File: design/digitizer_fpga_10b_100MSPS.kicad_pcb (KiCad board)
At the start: 4 copper layers, 110 x 60 mm, 281 parts, among them J1 POWER, J2 SWD_01X04, J3 DEBUG_SPI, J4 USB_B_Mini, J5 SMA, J6 JUMPER_DFS/GAIN, J7 DEBUG_FPGA_GPIO, J8 DIGILENT_JTAG_HS2_01X06, SW1 RST, SW2 PROG, U1 LM3880MF-1AA, U10 IS61WV12816EDBLL-10TLI, U11 TLV431ACDBZR, U12 AD9214, U13 XC7S15-FTGB196, U14 IS25LP064A-JKx, U2 NCP59744MN1, U3 NCP59744MN1, U4 NCP59744MN1, U5 NCP59744MN1, U6 STM32H750VBTx, U7 USBLC6-2SC6, U8 FT231XS, U9 ADA4930-1, X1 ASTX-H11-25.000MHZ-T

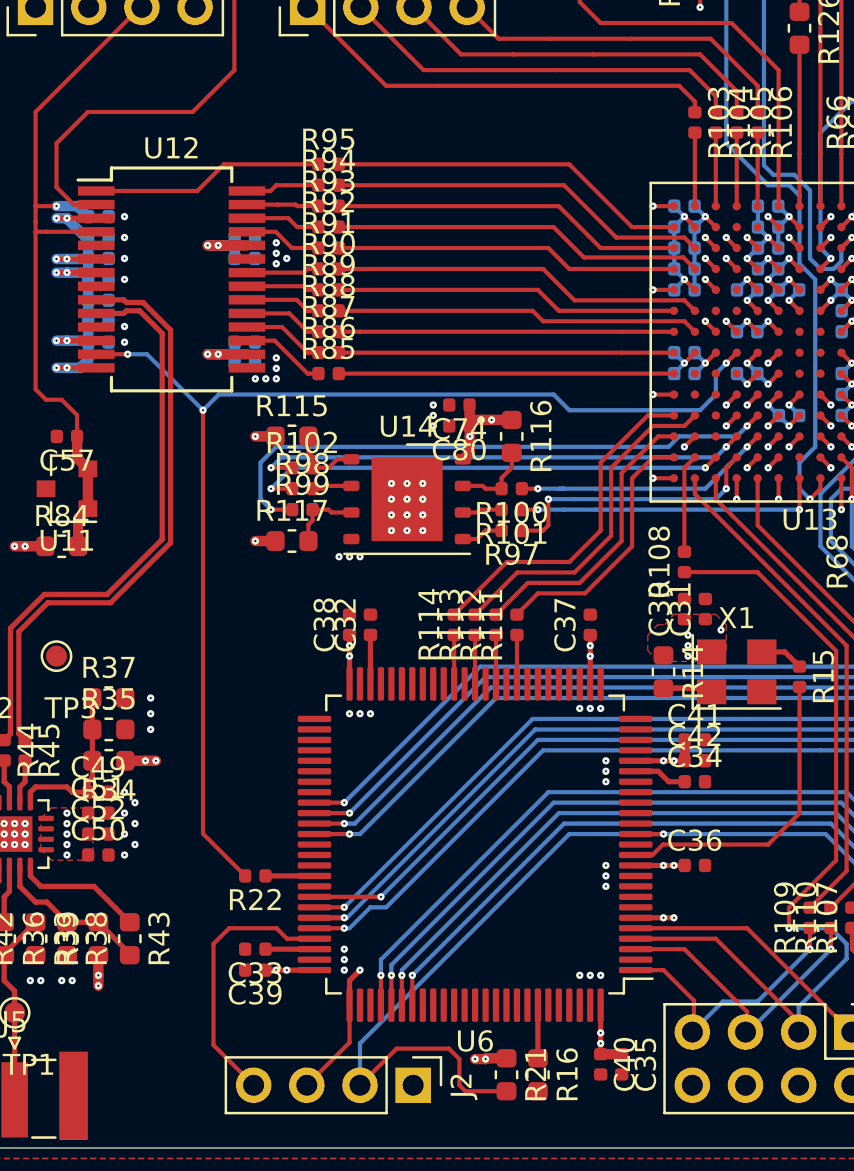
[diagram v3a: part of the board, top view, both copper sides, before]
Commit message: Connected reset to FPGA
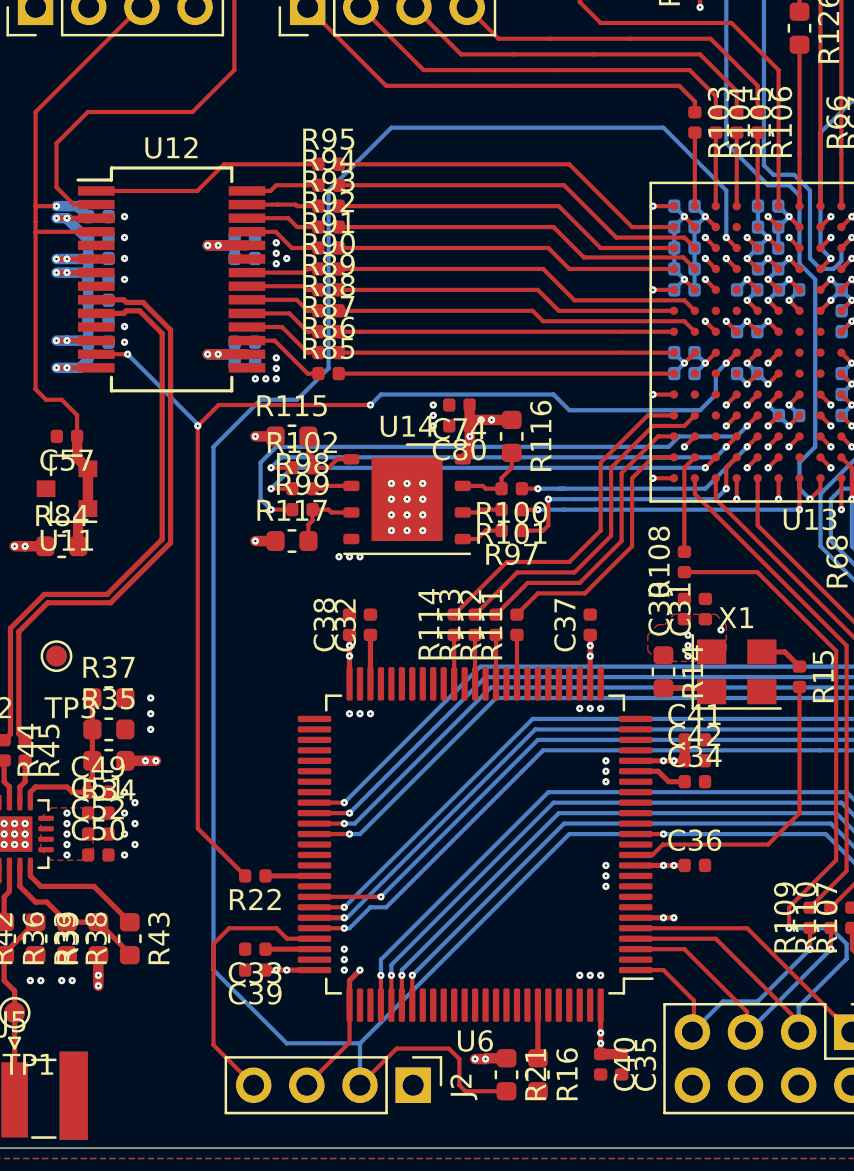
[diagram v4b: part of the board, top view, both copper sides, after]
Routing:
- net /~RST: track 51.1 -> 123.8 mm
- net /CLK: track 57.1 -> 57.2 mm, vias 3 -> 4
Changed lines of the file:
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@@
     (thickness 1.628)
     (drawings 36)
-    (tracks 1890)
+    (tracks 1905)
     (modules 281)
     (nets 334)
@@
       (dielectric_constraints yes)
     )
-    (last_trace_width 0.5)
+    (last_trace_width 0.2)
     (user_trace_width 0.2)
     (user_trace_width 0.5)
@@
   (gr_line (start 75 90) (end 175 90) (layer "Edge.Cuts") (width 0.05))
   (gr_line (start 70 145) (end 70 95) (layer "Edge.Cuts") (width 0.05))
+  (segment (start 115 112.75) (end 113.5 114.25) (width 0.2) (layer "BOT") (net 10))
+  (segment (start 118 101.25) (end 115 104.25) (width 0.2) (layer "BOT") (net 10))
+  (segment (start 109.5 141.5) (end 113 145) (width 0.2) (layer "BOT") (net 10))
+  (segment (start 115 104.25) (end 115 112.75) (width 0.2) (layer "BOT") (net 10))
+  (segment (start 131 101.25) (end 118 101.25) (width 0.2) (layer "BOT") (net 10))
+  (segment (start 134 106.5) (end 134 104.25) (width 0.2) (layer "BOT") (net 10))
+  (segment (start 134 104.25) (end 131 101.25) (width 0.2) (layer "BOT") (net 10))
+  (segment (start 113.5 114.25) (end 111.75 114.25) (width 0.2) (layer "BOT") (net 10))
+  (segment (start 111.75 114.25) (end 109.5 116.5) (width 0.2) (layer "BOT") (net 10))
+  (segment (start 109.5 116.5) (end 109.5 141.5) (width 0.2) (layer "BOT") (net 10))
+  (segment (start 113 145) (end 116.5 145) (width 0.2) (layer "BOT") (net 10))
+  (segment (start 109.5 114.75) (end 109.75 114.5) (width 0.2) (layer "TOP") (net 46))
+  (segment (start 108.75 115.5) (end 109.5 114.75) (width 0.2) (layer "TOP") (net 46))
+  (via (at 117 114.5) (size 0.35) (drill 0.1) (layers "TOP" "BOT") (net 46))
+  (segment (start 117 114.5) (end 117.5 114) (width 0.2) (layer "BOT") (net 46))
+  (segment (start 109.75 114.5) (end 117 114.5) (width 0.2) (layer "TOP") (net 46))
+  (segment (start 117.5 114) (end 125.75 114) (width 0.2) (layer "BOT") (net 46))
+  (segment (start 111.015 137) (end 108.75 134.735) (width 0.2) (layer "TOP") (net 46))
+  (segment (start 108.75 134.735) (end 108.75 115.5) (width 0.2) (layer "TOP") (net 46))
+  (segment (start 108.75 115.425) (end 108.75 115.5) (width 0.2) (layer "BOT") (net 46))
+  (segment (start 105.4 112.075) (end 108.75 115.425) (width 0.2) (layer "BOT") (net 46))
+  (via (at 108.75 115.5) (size 0.35) (drill 0.1) (layers "TOP" "BOT") (net 46))
   (segment (start 112.4625 121) (end 111.5 121) (width 0.5) (layer "TOP") (net 2))
   (via (at 111.5 121) (size 0.35) (drill 0.1) (layers "TOP" "BOT") (net 2))
@@
   (segment (start 121.75 116.7575) (end 121.75 116) (width 0.5) (layer "TOP") (net 2))
   (segment (start 121.75 115.515) (end 121.735 115.5) (width 0.5) (layer "TOP") (net 2))
-  (segment (start 125.75 114) (end 109.75 114) (width 0.2) (layer "BOT") (net 46))
   (segment (start 126.5 114.75) (end 125.75 114) (width 0.2) (layer "BOT") (net 46))
   (segment (start 132.75 114.75) (end 126.5 114.75) (width 0.2) (layer "BOT") (net 46))
@@
   (segment (start 133.5 114) (end 132.75 114.75) (width 0.2) (layer "BOT") (net 46))
   (segment (start 133.5 113) (end 133.5 114) (width 0.2) (layer "BOT") (net 46))
-  (segment (start 109.75 114) (end 109 114.75) (width 0.2) (layer "BOT") (net 46))
   (segment (start 114.235 117.5) (end 114.235 116.985) (width 0.2) (layer "TOP") (net 92))
   (segment (start 114.235 116.985) (end 114.0375 116.7875) (width 0.2) (layer "TOP") (net 92))
@@
   (segment (start 116 143.175) (end 116 144.96) (width 0.2) (layer "TOP") (net 19))
   (segment (start 116 144.96) (end 113.96 147) (width 0.2) (layer "TOP") (net 19))
-  (segment (start 111.015 137) (end 109 134.985) (width 0.2) (layer "TOP") (net 46))
-  (segment (start 109 134.985) (end 109 114.75) (width 0.2) (layer "TOP") (net 46))
-  (segment (start 106.325 112.075) (end 109 114.75) (width 0.2) (layer "BOT") (net 46))
-  (segment (start 105.4 112.075) (end 106.325 112.075) (width 0.2) (layer "BOT") (net 46))
-  (via (at 109 114.75) (size 0.35) (drill 0.1) (layers "TOP" "BOT") (net 46))
   (via (at 105.4 112.075) (size 0.35) (drill 0.1) (layers "TOP" "BOT") (net 46) (status 40000))
   (segment (start 103.9 112.075) (end 105.4 112.075) (width 0.2) (layer "TOP") (net 46))

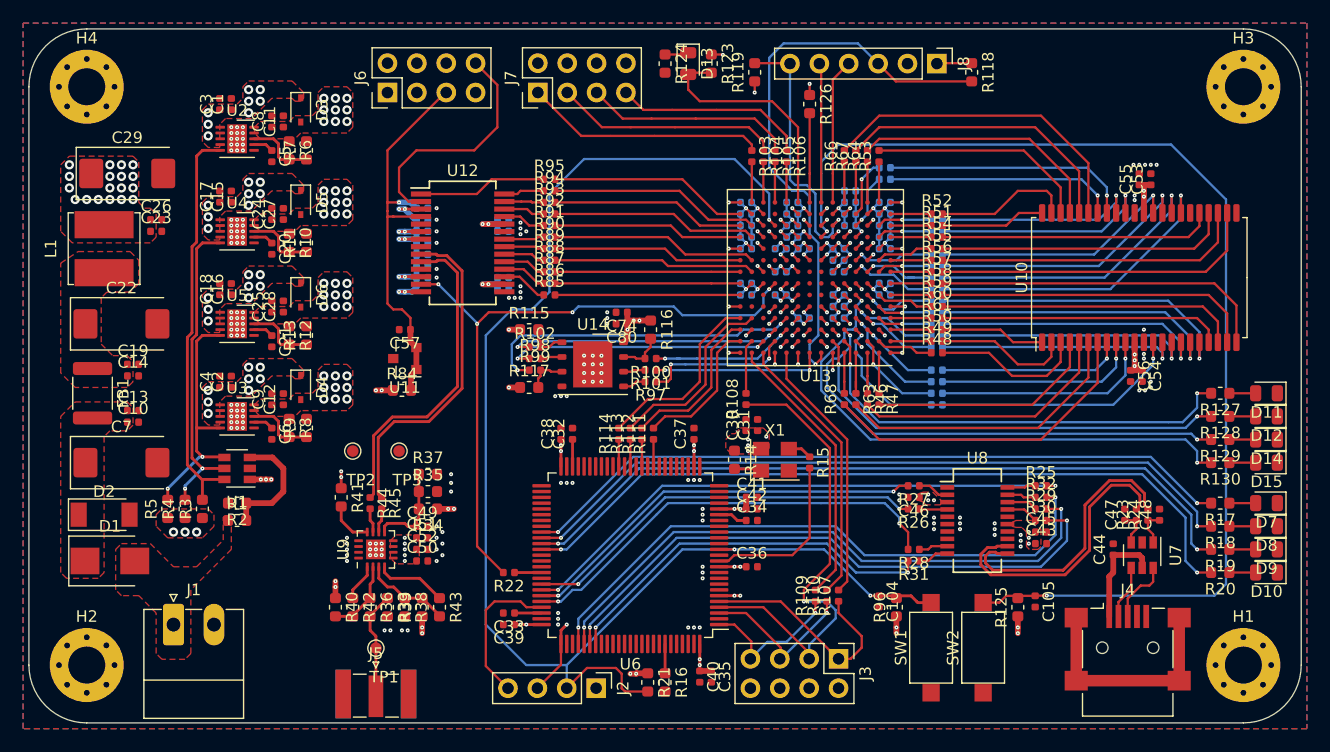
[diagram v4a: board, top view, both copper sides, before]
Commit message: Connected FPGA controll
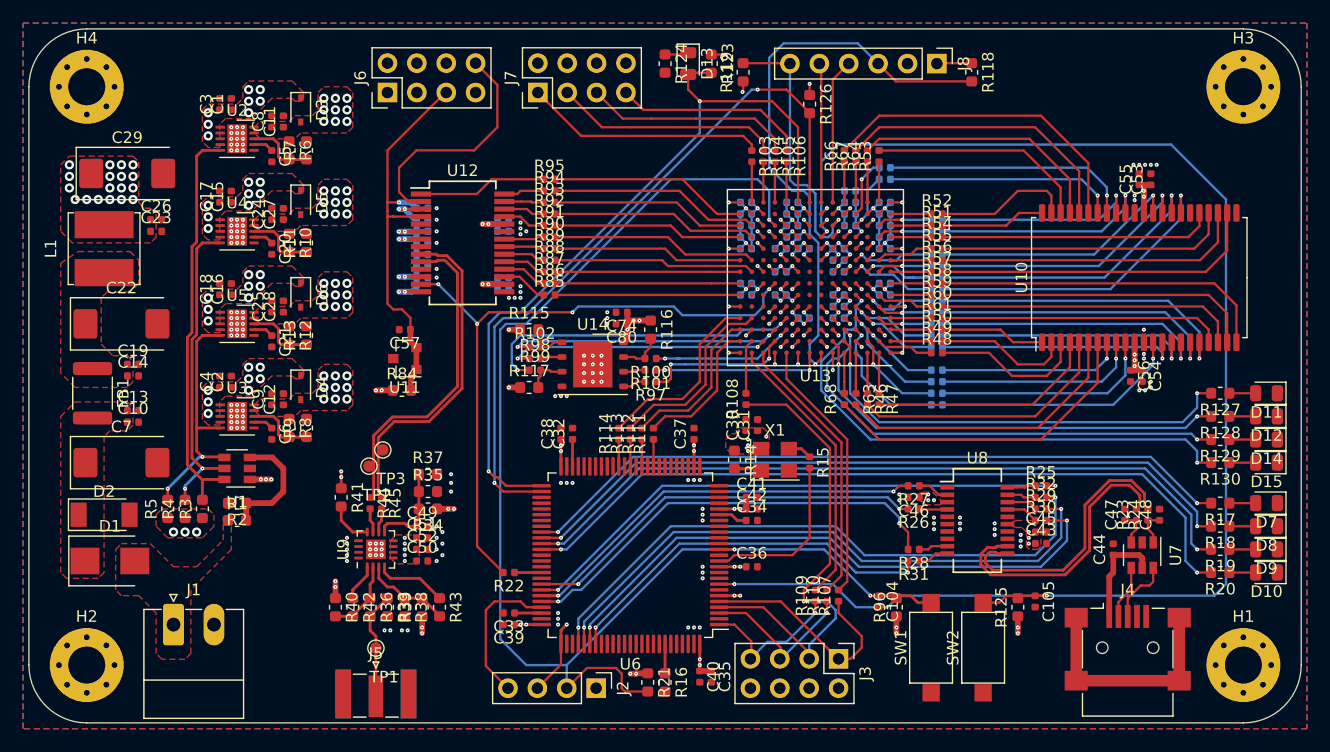
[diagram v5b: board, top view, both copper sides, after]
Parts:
- moved TP2 1.91 mm to (99.4, 127.8)
- moved TP3 1.40 mm to (100.6, 126.4)
- moved R119 1.00 mm to (131.8, 93.8)
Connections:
- U6 pad 51: Net-(U6-Pad51) -> /FPGA_DONE
- U6 pad 52: Net-(U6-Pad52) -> /FPGA_ERROR
- U6 pad 8: Net-(U6-Pad8) -> /FPGA_LOAD_BITSTREAM
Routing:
- net /FPGA_ERROR: track 7.71 -> 62.2 mm, vias 0 -> 2
- net /FPGA_DONE: track 20.7 -> 66.4 mm, vias 0 -> 2
- net /FPGA_LOAD_BITSTREAM: track 99.6 -> 129.2 mm, vias 2 -> 3
- net /~RST: track 123.8 -> 116.1 mm
- net /FPGA/TMS: track 23.0 -> 24.0 mm

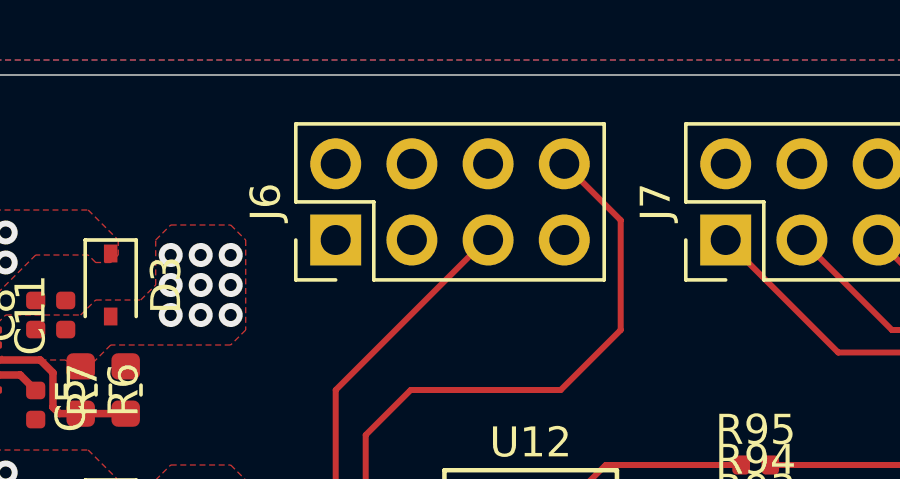
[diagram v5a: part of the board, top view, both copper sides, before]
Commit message: Connected ADC jumper
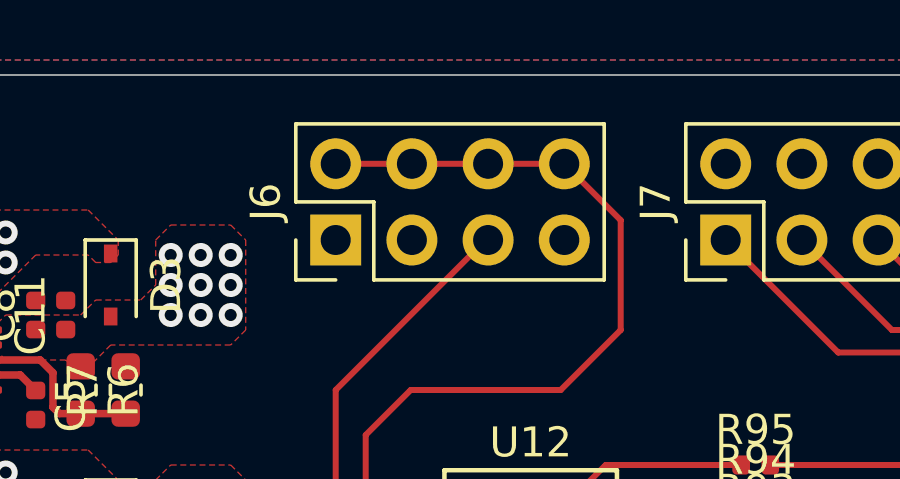
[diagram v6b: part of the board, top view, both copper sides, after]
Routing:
- net Net-(J6-Pad2): track 20.6 -> 28.2 mm
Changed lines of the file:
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@@
     (thickness 1.628)
     (drawings 36)
-    (tracks 1935)
+    (tracks 1938)
     (modules 281)
     (nets 331)
@@
   (gr_line (start 75 90) (end 175 90) (layer "Edge.Cuts") (width 0.05))
   (gr_line (start 70 145) (end 70 95) (layer "Edge.Cuts") (width 0.05))
+  (segment (start 103.54 92.96) (end 101 92.96) (width 0.2) (layer "TOP") (net 24))
+  (segment (start 106.08 92.96) (end 103.54 92.96) (width 0.2) (layer "TOP") (net 24))
+  (segment (start 108.62 92.96) (end 106.08 92.96) (width 0.2) (layer "TOP") (net 24))
   (segment (start 132.5 95.25) (end 112.75 115) (width 0.2) (layer "BOT") (net 307))
   (segment (start 112.75 115) (end 111 115) (width 0.2) (layer "BOT") (net 307))

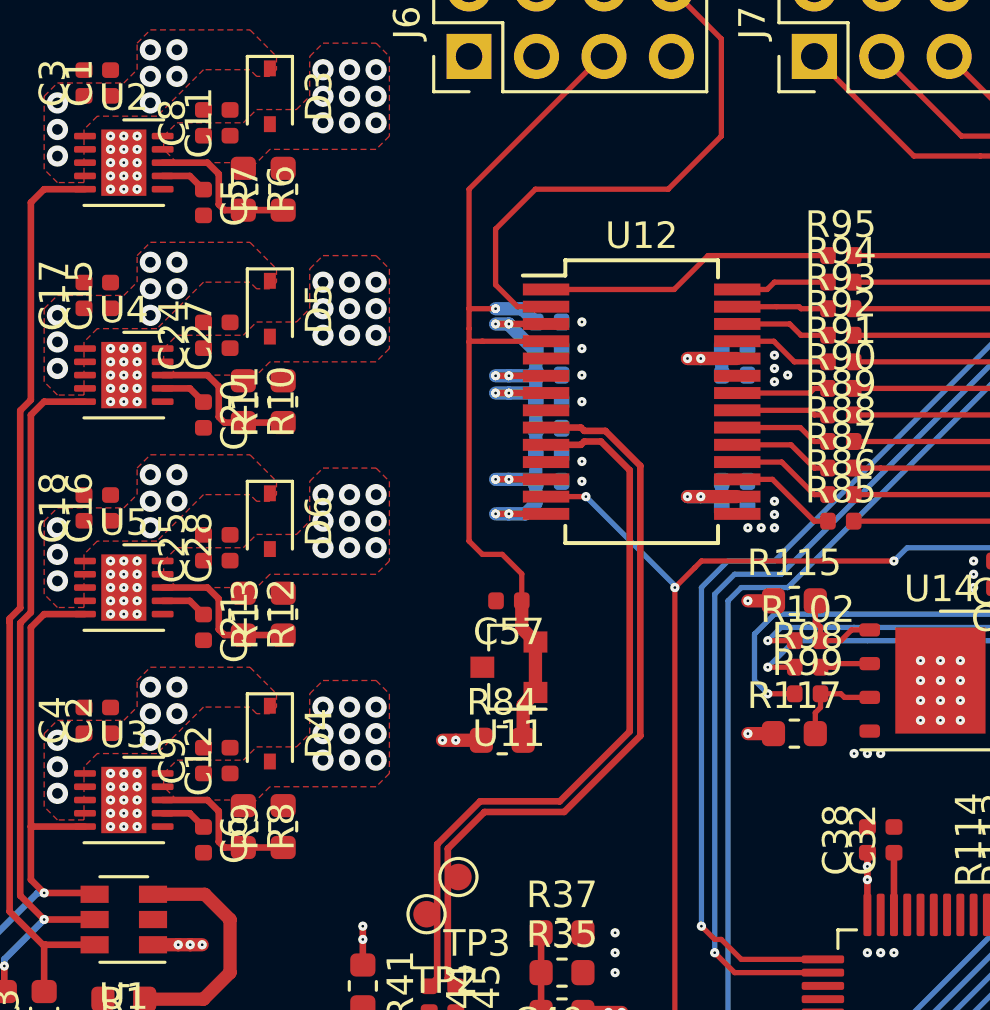
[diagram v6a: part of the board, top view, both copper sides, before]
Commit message: Fixed some design rules
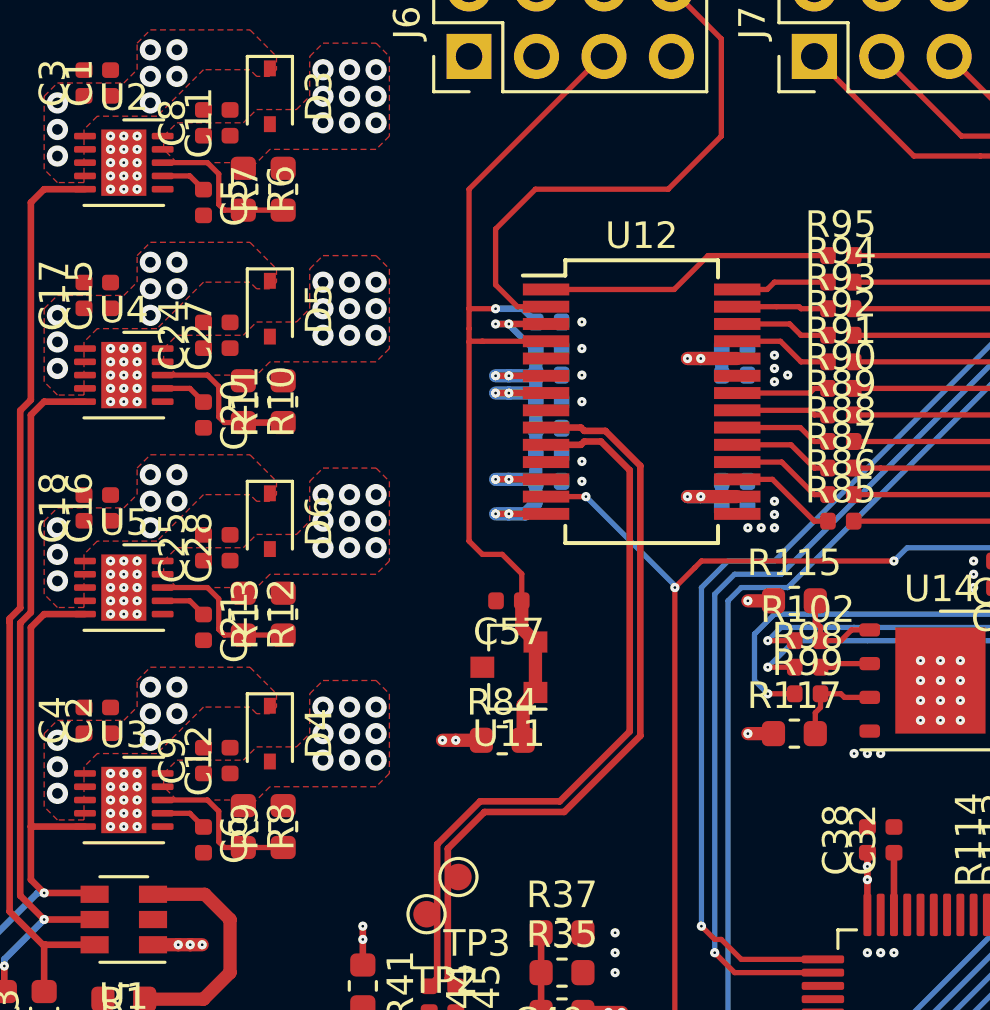
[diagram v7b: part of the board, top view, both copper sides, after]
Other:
- net class Default: clearance 0.15 -> 0.125
- rule trace_clearance: 0.15 -> 0.125
